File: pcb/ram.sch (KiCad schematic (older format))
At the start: 7 parts, among them U1 AS4C512M16D3L-12BIN

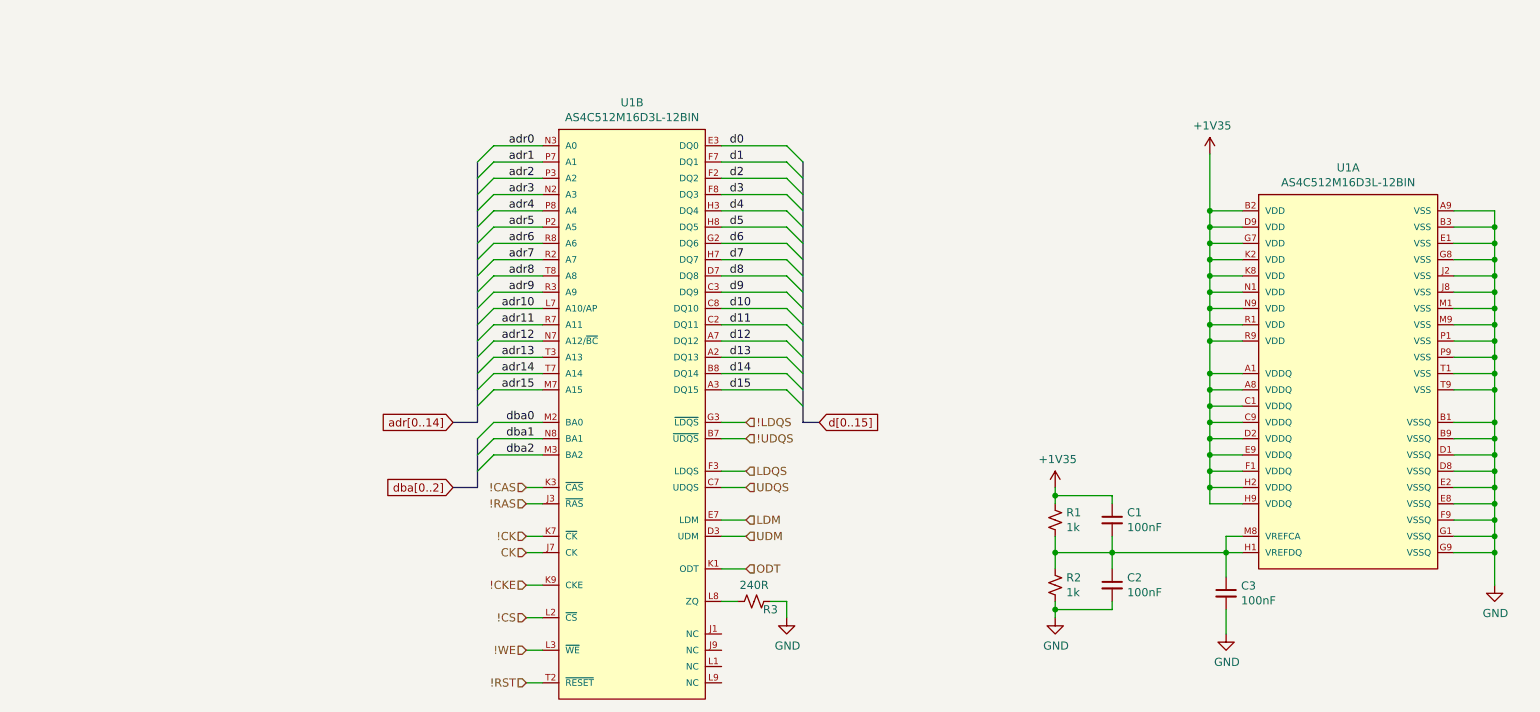
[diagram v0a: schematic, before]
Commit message: Decoupled the ram and A33
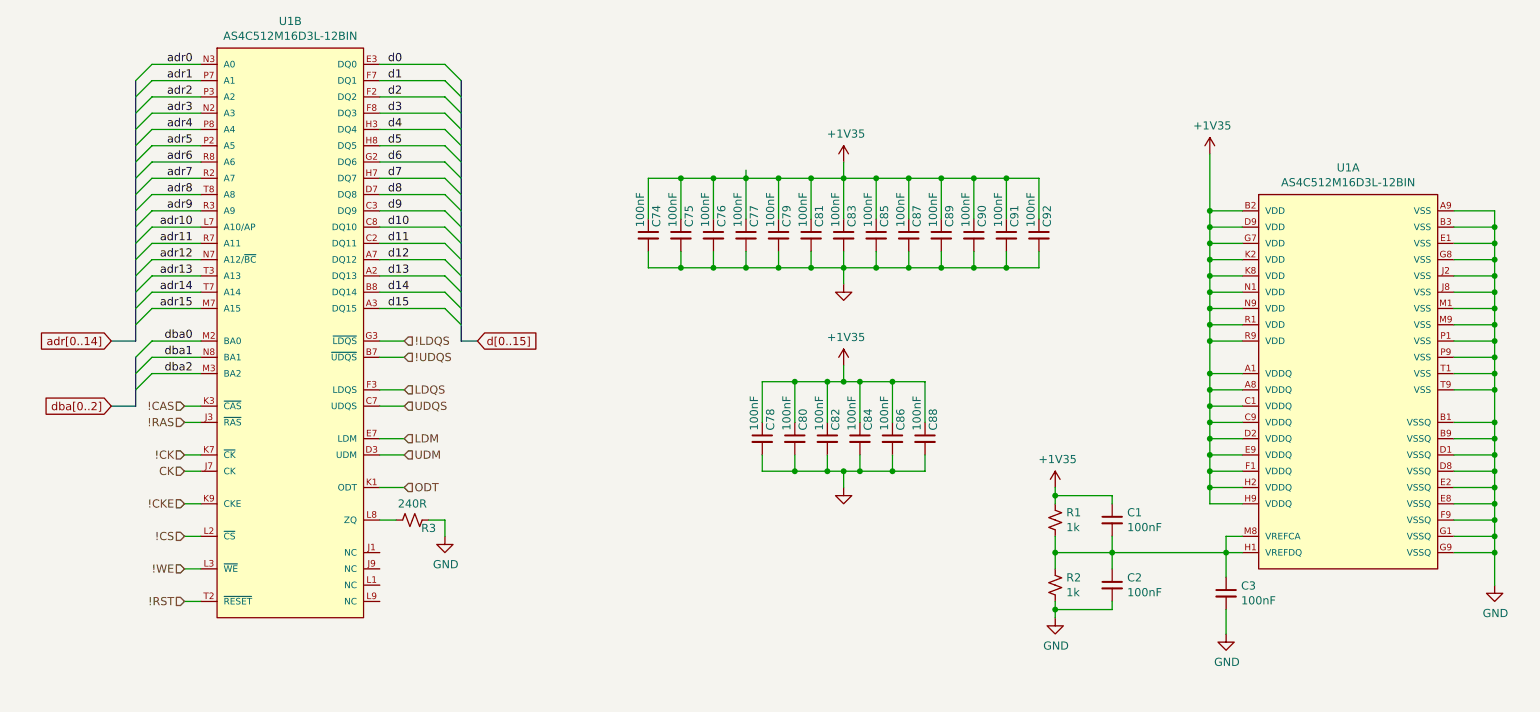
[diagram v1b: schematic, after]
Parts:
- added C74, C75, C76, C77, C78, C79, C80, C81, C82, C83, C84, C85, C86, C87, C88, C89, C90, C91, C92: 100nF, Capacitor_SMD:C_01005_0402Metric, symbol Device:C_Small
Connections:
- net +1V35: now also C74.1, C75.1, C76.1, C77.1, C78.1, C79.1, C80.1, C81.1, C82.1, C83.1, C84.1, C85.1, C86.1, C87.1, C88.1, C89.1, C90.1, C91.1, C92.1
- net GND: now also C74.2, C75.2, C76.2, C77.2, C78.2, C79.2, C80.2, C81.2, C82.2, C83.2, C84.2, C85.2, C86.2, C87.2, C88.2, C89.2, C90.2, C91.2, C92.2
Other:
- moved on the sheet: R3, U1B

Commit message: Backing up
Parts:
- C1, C2, C3, C74, C75, C76, C77, C78, C79, C80, C81, C82, C83, C84, C85, C86, C87, C88, C89, C90, C91, C92: footprint Capacitor_SMD:C_01005_0402Metric -> Capacitor_SMD:C_0402_1005Metric
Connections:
- net labels added: adr[0..15]
- net labels removed: adr[0..14]

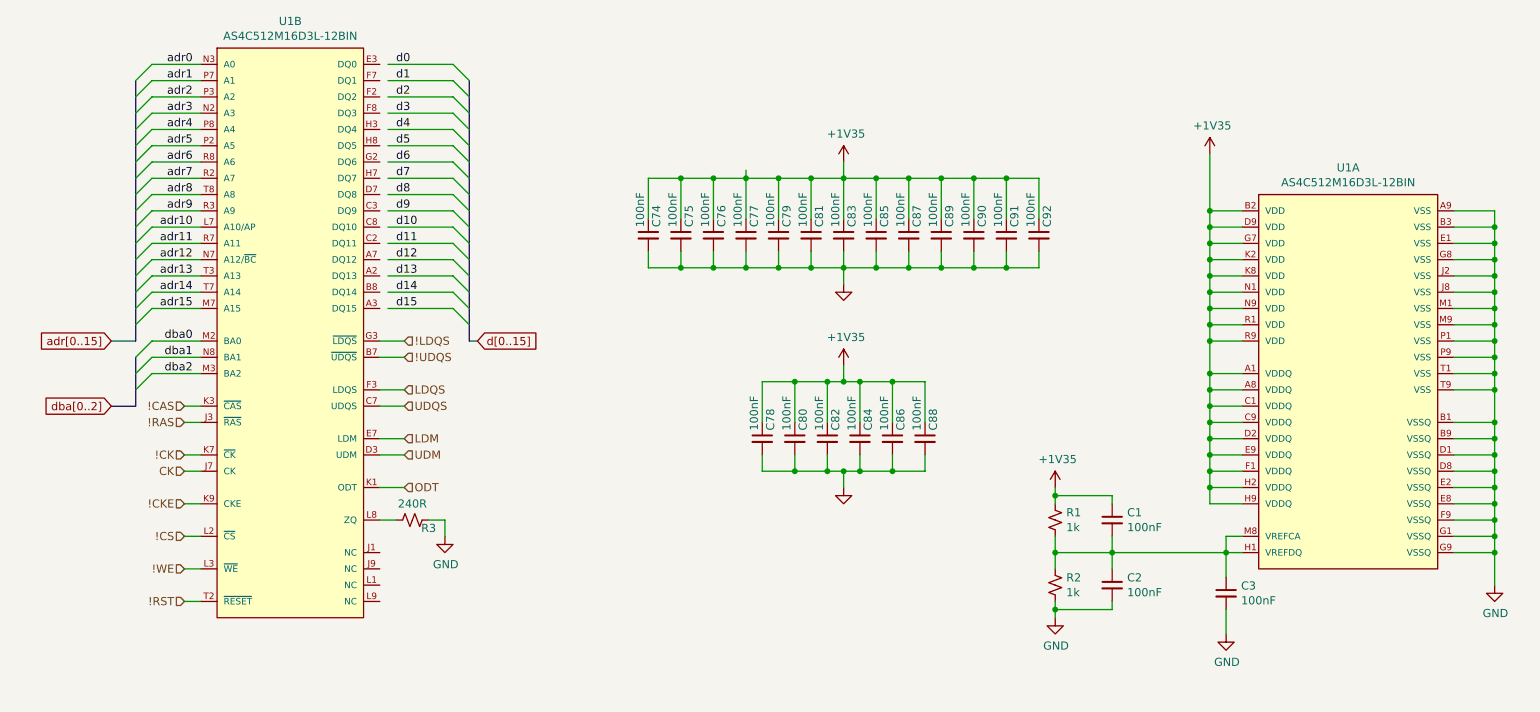
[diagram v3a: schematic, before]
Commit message: Repositioned the ram.
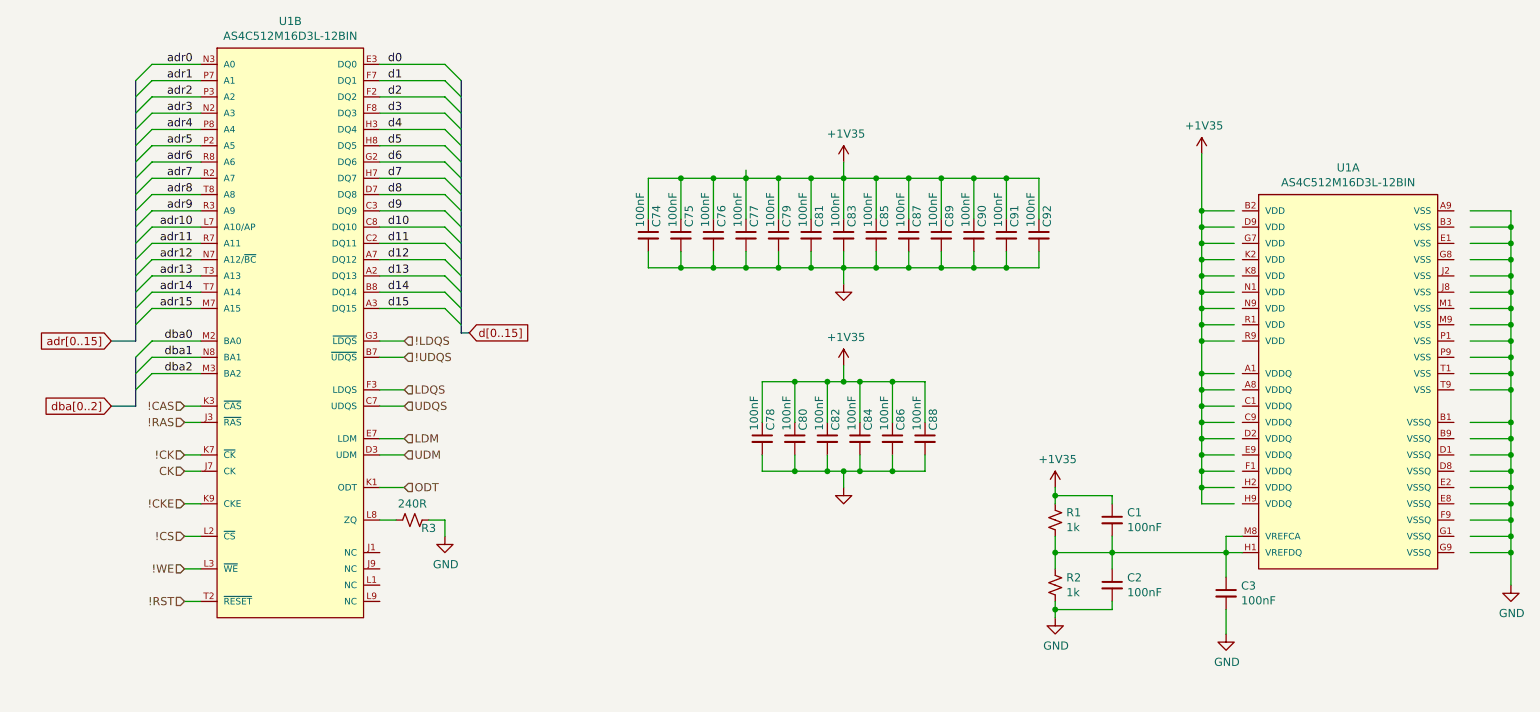
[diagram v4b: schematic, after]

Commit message: RAM hooked up
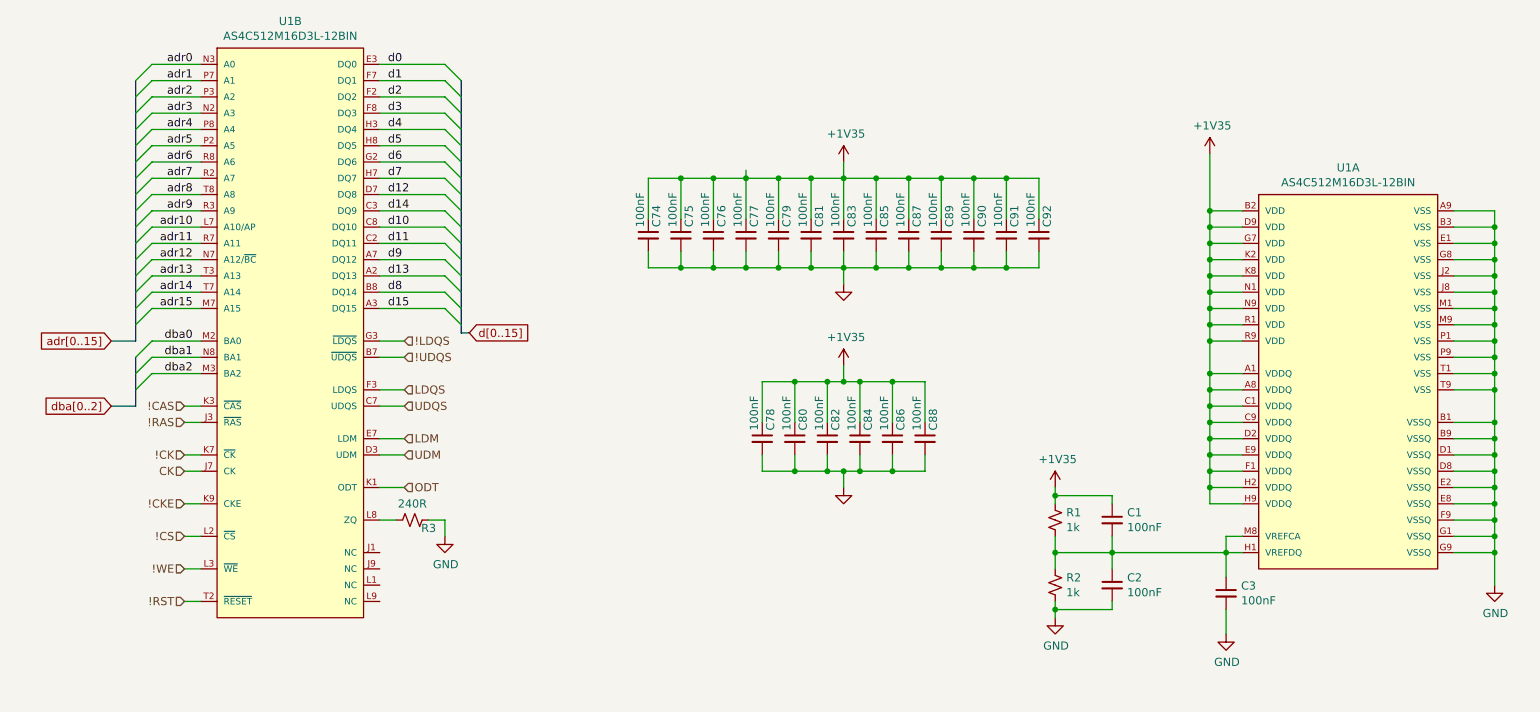
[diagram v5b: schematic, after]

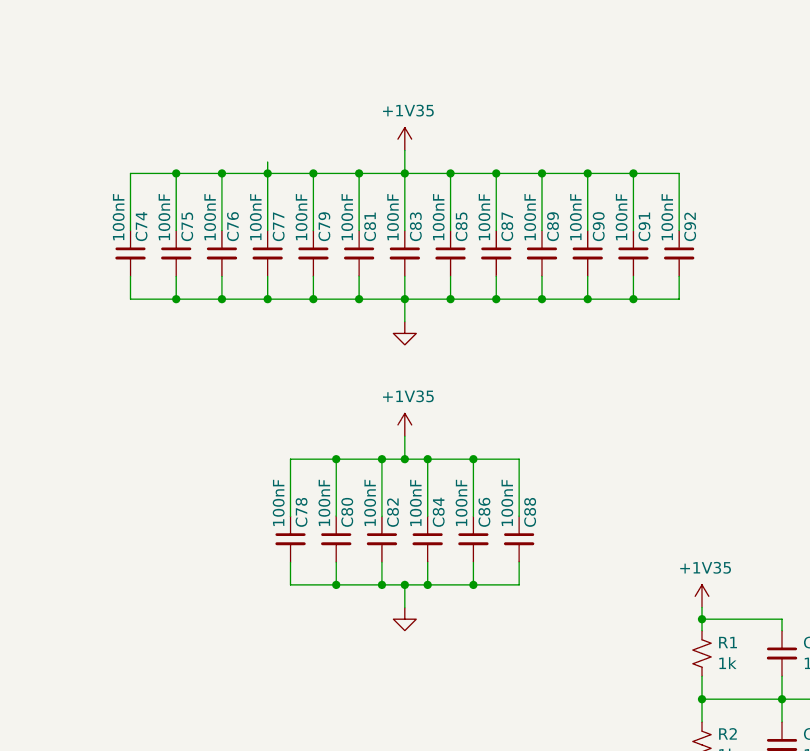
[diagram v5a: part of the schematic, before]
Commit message: Ram finally hooked up
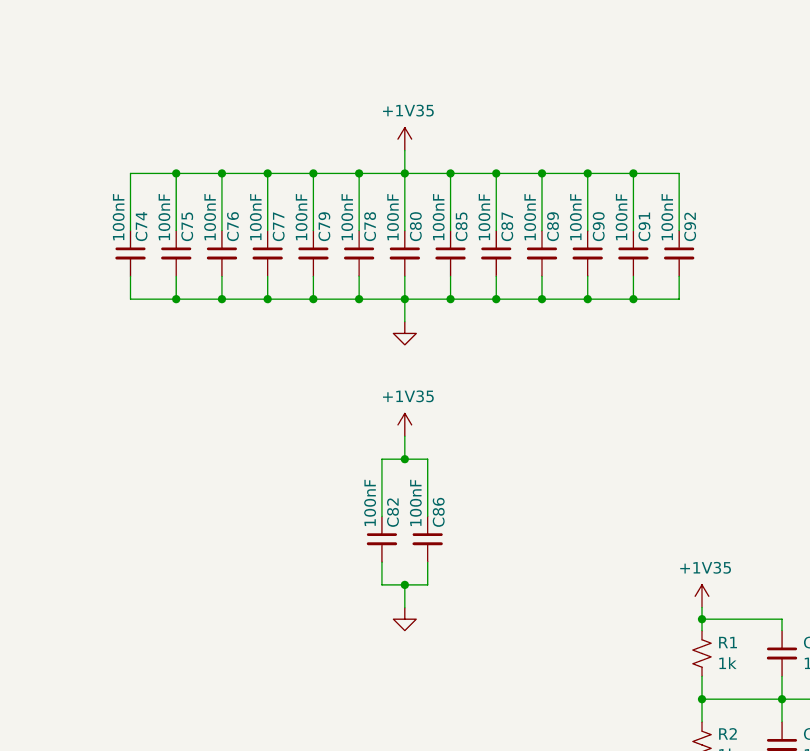
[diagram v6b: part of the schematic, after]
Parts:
- removed C81, C83, C84, C88: 100nF, Capacitor_SMD:C_0402_1005Metric, symbol Device:C_Small
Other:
- moved on the sheet: C78, C80, C86
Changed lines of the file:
@@
 Wire Wire Line
 	4600 1950 4800 1950
-Wire Wire Line
-	5200 1950 5200 1900
 $Comp
 L Device:C_Small C75
@@
 F 3 "~" H 5400 2300 50  0001 C CNN
 	1    5400 2300
-	1    0    0    -1
-$EndComp
-$Comp
-L Device:C_Small C81
-U 1 1 60D3E7EE
-P 5600 2300
-AR Path="/60536DA4/60D3E7EE" Ref="C81"  Part="1"
-AR Path="/60D3E7EE" Ref="C?"  Part="1"
-F 0 "C81" V 5650 2350 50  0000 L CNN
-F 1 "100nF" V 5550 2350 50  0000 L CNN
-F 2 "Capacitor_SMD:C_0402_1005Metric" H 5600 2300 50  0001 C CNN
-F 3 "~" H 5600 2300 50  0001 C CNN
-	1    5600 2300
 	1    0    0    -1
 $EndComp
@@
 Wire Wire Line
 	5800 2600 5800 2500
-$Comp
-L Device:C_Small C83
-U 1 1 60D48397
-P 5800 2300
-AR Path="/60536DA4/60D48397" Ref="C83"  Part="1"
-AR Path="/60D48397" Ref="C?"  Part="1"
-F 0 "C83" V 5850 2350 50  0000 L CNN
-F 1 "100nF" V 5750 2350 50  0000 L CNN
-F 2 "Capacitor_SMD:C_0402_1005Metric" H 5800 2300 50  0001 C CNN
-F 3 "~" H 5800 2300 50  0001 C CNN
-	1    5800 2300
-	1    0    0    -1
-$EndComp
 $Comp
 L Device:C_Small C85
@@
 L Device:C_Small C78
 U 1 1 60DC9101
-P 5300 3550
+P 5600 2300
 AR Path="/60536DA4/60DC9101" Ref="C78"  Part="1"
 AR Path="/60DC9101" Ref="C?"  Part="1"
-F 0 "C78" V 5350 3600 50  0000 L CNN
-F 1 "100nF" V 5250 3600 50  0000 L CNN
-F 2 "Capacitor_SMD:C_0402_1005Metric" H 5300 3550 50  0001 C CNN
-F 3 "~" H 5300 3550 50  0001 C CNN
-	1    5300 3550
+F 0 "C78" V 5650 2350 50  0000 L CNN
+F 1 "100nF" V 5550 2350 50  0000 L CNN
+F 2 "Capacitor_SMD:C_0402_1005Metric" H 5600 2300 50  0001 C CNN
+F 3 "~" H 5600 2300 50  0001 C CNN
+	1    5600 2300
 	1    0    0    -1
 $EndComp
@@
 L Device:C_Small C80
 U 1 1 60DC9107
-P 5500 3550
+P 5800 2300
 AR Path="/60536DA4/60DC9107" Ref="C80"  Part="1"
 AR Path="/60DC9107" Ref="C?"  Part="1"
-F 0 "C80" V 5550 3600 50  0000 L CNN
-F 1 "100nF" V 5450 3600 50  0000 L CNN
-F 2 "Capacitor_SMD:C_0402_1005Metric" H 5500 3550 50  0001 C CNN
-F 3 "~" H 5500 3550 50  0001 C CNN
-	1    5500 3550
+F 0 "C80" V 5850 2350 50  0000 L CNN
+F 1 "100nF" V 5750 2350 50  0000 L CNN
+F 2 "Capacitor_SMD:C_0402_1005Metric" H 5800 2300 50  0001 C CNN
+F 3 "~" H 5800 2300 50  0001 C CNN
+	1    5800 2300
 	1    0    0    -1
 $EndComp
@@
 $EndComp
 $Comp
-L Device:C_Small C84
-U 1 1 60DC9113
+L Device:C_Small C86
+U 1 1 60DC9119
 P 5900 3550
-AR Path="/60536DA4/60DC9113" Ref="C84"  Part="1"
-AR Path="/60DC9113" Ref="C?"  Part="1"
-F 0 "C84" V 5950 3600 50  0000 L CNN
+AR Path="/60536DA4/60DC9119" Ref="C86"  Part="1"
+AR Path="/60DC9119" Ref="C?"  Part="1"
+F 0 "C86" V 5950 3600 50  0000 L CNN
 F 1 "100nF" V 5850 3600 50  0000 L CNN
 F 2 "Capacitor_SMD:C_0402_1005Metric" H 5900 3550 50  0001 C CNN
@@
 	1    0    0    -1
 $EndComp
-$Comp
-L Device:C_Small C86
-U 1 1 60DC9119
-P 6100 3550
-AR Path="/60536DA4/60DC9119" Ref="C86"  Part="1"
-AR Path="/60DC9119" Ref="C?"  Part="1"
-F 0 "C86" V 6150 3600 50  0000 L CNN
-F 1 "100nF" V 6050 3600 50  0000 L CNN
-F 2 "Capacitor_SMD:C_0402_1005Metric" H 6100 3550 50  0001 C CNN
-F 3 "~" H 6100 3550 50  0001 C CNN
-	1    6100 3550
-	1    0    0    -1
-$EndComp
-Wire Wire Line
-	6100 3450 6100 3200
 Wire Wire Line
 	5900 3450 5900 3200
 Wire Wire Line
-	5700 3450 5700 3200
-Wire Wire Line
-	5500 3450 5500 3200
-Wire Wire Line
-	5300 3450 5300 3200
-Wire Wire Line
-	6300 3750 6300 3650
-Wire Wire Line
-	6100 3650 6100 3750
-Wire Wire Line
 	5900 3650 5900 3750
 Wire Wire Line
 	5700 3650 5700 3750
-Wire Wire Line
-	5500 3650 5500 3750
-Wire Wire Line
-	5300 3650 5300 3750
-$Comp
-L Device:C_Small C88
-U 1 1 60DC912A
-P 6300 3550
-AR Path="/60536DA4/60DC912A" Ref="C88"  Part="1"
-AR Path="/60DC912A" Ref="C?"  Part="1"
-F 0 "C88" V 6350 3600 50  0000 L CNN
-F 1 "100nF" V 6250 3600 50  0000 L CNN
-F 2 "Capacitor_SMD:C_0402_1005Metric" H 6300 3550 50  0001 C CNN
-F 3 "~" H 6300 3550 50  0001 C CNN
-	1    6300 3550
-	1    0    0    -1
-$EndComp
-Wire Wire Line
-	6300 3200 6300 3450
 $Comp
 L power:+1V35 #PWR065
@@
 $EndComp
 Wire Wire Line
-	5300 3200 5500 3200
-Connection ~ 5500 3200
-Wire Wire Line
-	5500 3200 5700 3200
-Connection ~ 5700 3200
-Wire Wire Line
 	5700 3200 5800 3200
-Connection ~ 5900 3200
-Wire Wire Line
-	5900 3200 6100 3200
-Connection ~ 6100 3200
-Wire Wire Line
-	6100 3200 6300 3200
 Wire Wire Line
 	5800 3200 5800 3100
@@
 $EndComp
 Wire Wire Line
-	5300 3750 5500 3750
-Connection ~ 5500 3750
-Wire Wire Line
-	5500 3750 5700 3750
-Connection ~ 5700 3750
-Wire Wire Line
 	5700 3750 5800 3750
-Connection ~ 5900 3750
-Wire Wire Line
-	5900 3750 6100 3750
-Connection ~ 6100 3750
-Wire Wire Line
-	6100 3750 6300 3750
 Wire Wire Line
 	5800 3750 5800 3850
@@
 Wire Wire Line
 	9550 2150 9800 2150
+Wire Wire Line
+	5700 3450 5700 3200
 Wire Bus Line
 	1450 3050 1450 3350
